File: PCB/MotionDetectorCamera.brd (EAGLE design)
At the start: 41.9 x 32.6 mm, 185 parts, among them J1 JUMPER-SOLDER, J10 MICROSD-SOCKET, J11 USB-C-JACK, J2 JUMPER-SOLDER, J3 JUMPER-SOLDER, J4 JUMPER-SOLDER, J5 JST-SM02B-SRSS-TB, J6 JUMPER-SOLDER, J7 JUMPER-SOLDER, J8 JUMPER-SOLDER, J9 S-MOUNT-LENS-HOLDERM12LENSES-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, Q1 PMOS-NEXPERIA-SOT1220, Q2 PMOS-NEXPERIA-SOT1220, Q3 PMOS-NEXPERIA-SOT1220, U1 TI-TPS2116, U10 TI-TPS22919DCK, U11 TI-TPS62A01, U13 TI-TPS22919DCK, U14 TI-TPS22919DCK, U15 TI-MSP430FR2422IRHL, U16 NXP-NTB0102, U17 NXP-NTB0102, U18 PANASONIC-EKMB110711X, U19 LATTICE-ICE40HX4K-BG121, U2 DIODESINC-AP7350, U20 WINBOND-W25Q40EW, U21 NEXPERIA-74LVC1G98-OR-INV-INP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, U22 NEXPERIA-74LVC1G98-BUFFER, U23 ON-AR0330CS1C12SPKA0, U24 ALLIANCE-AS4C8M16MSA-6BIN, U25 STM-STM32F730, U26 DIODESINC-DT1446-04V-7, U27 NEXPERIA-74LVC1G98-BUFFER, U3 NEXPERIA-74LVC1G98-NOR, U4 MICROCHIP-MCP7383X, U5 EATON-STN101, U6 TI-TPS62A01, U7 TI-TPS62A01, U9 TI-TPS22919DCK, X1 EPSON-FC-135, X2 SITIME-SIT8021, X3 SITIME-SIT8021

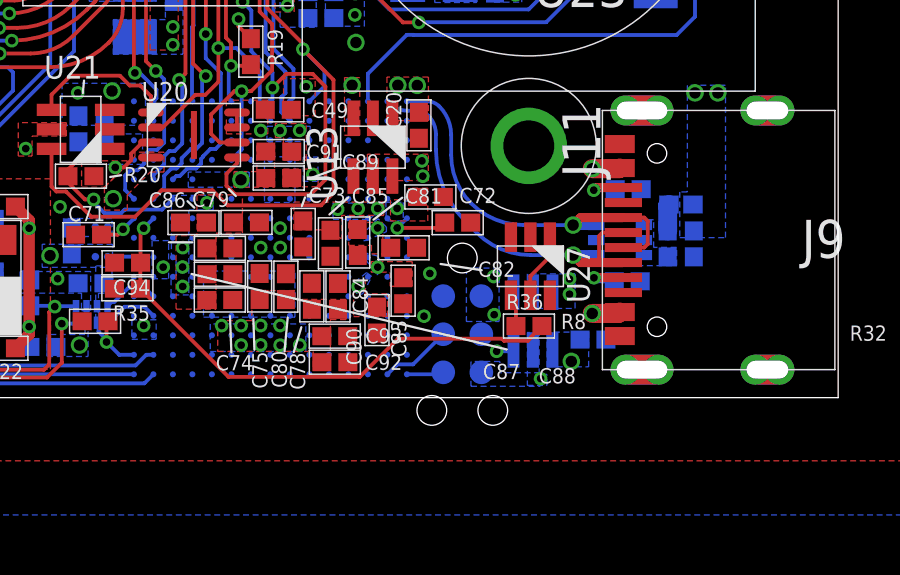
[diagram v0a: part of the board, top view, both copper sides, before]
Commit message: 39 airwires
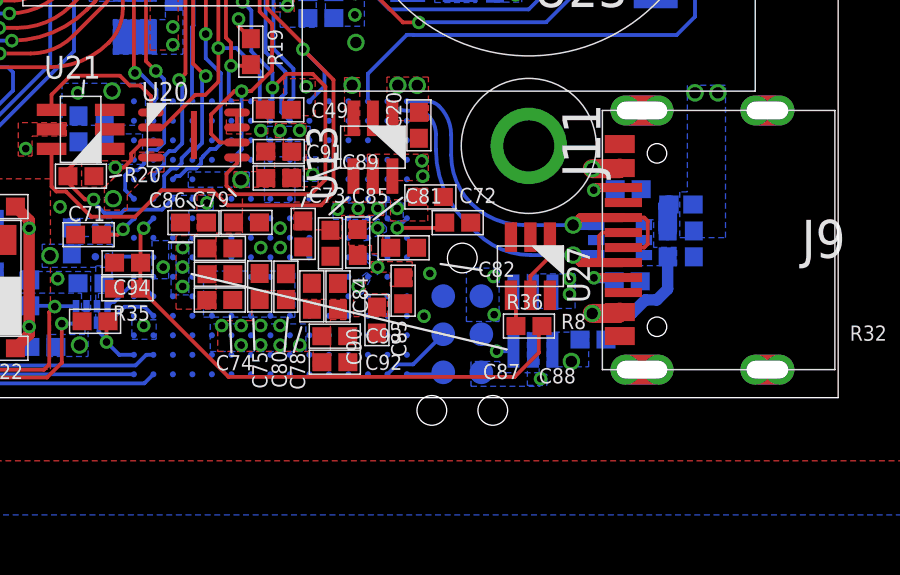
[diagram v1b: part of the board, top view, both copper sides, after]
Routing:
- net N$54: track 1.87 -> 11.4 mm
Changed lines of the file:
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@@
 <grid distance="10" unitdist="mil" unit="mil" style="lines" multiple="1" display="no" altdistance="0.00254" altunitdist="mm" altunit="mil"/>
 <layers>
-<layer number="1" name="Top" color="4" fill="1" visible="yes" active="yes"/>
+<layer number="1" name="Top" color="4" fill="1" visible="no" active="yes"/>
 <layer number="2" name="Ground" color="16" fill="1" visible="no" active="yes"/>
 <layer number="3" name="Route3" color="17" fill="1" visible="no" active="no"/>
@@
 <layer number="14" name="Route14" color="22" fill="1" visible="no" active="no"/>
 <layer number="15" name="Power" color="42" fill="1" visible="no" active="yes"/>
-<layer number="16" name="Bottom" color="1" fill="1" visible="no" active="yes"/>
+<layer number="16" name="Bottom" color="1" fill="1" visible="yes" active="yes"/>
 <layer number="17" name="Pads" color="2" fill="1" visible="yes" active="yes"/>
 <layer number="18" name="Vias" color="2" fill="1" visible="yes" active="yes"/>
 <layer number="19" name="Unrouted" color="6" fill="1" visible="no" active="yes"/>
 <layer number="20" name="Dimension" color="24" fill="1" visible="yes" active="yes"/>
-<layer number="21" name="tPlace" color="7" fill="1" visible="yes" active="yes"/>
-<layer number="22" name="bPlace" color="7" fill="1" visible="no" active="yes"/>
-<layer number="23" name="tOrigins" color="15" fill="1" visible="yes" active="yes"/>
-<layer number="24" name="bOrigins" color="15" fill="1" visible="no" active="yes"/>
-<layer number="25" name="tNames" color="7" fill="1" visible="yes" active="yes"/>
-<layer number="26" name="bNames" color="7" fill="1" visible="no" active="yes"/>
-<layer number="27" name="tValues" color="7" fill="1" visible="yes" active="yes"/>
-<layer number="28" name="bValues" color="7" fill="1" visible="no" active="yes"/>
-<layer number="29" name="tStop" color="7" fill="3" visible="yes" active="yes"/>
-<layer number="30" name="bStop" color="7" fill="6" visible="no" active="yes"/>
-<layer number="31" name="tCream" color="7" fill="4" visible="yes" active="yes"/>
-<layer number="32" name="bCream" color="7" fill="5" visible="no" active="yes"/>
-<layer number="33" name="tFinish" color="6" fill="3" visible="yes" active="yes"/>
-<layer number="34" name="bFinish" color="6" fill="6" visible="no" active="yes"/>
-<layer number="35" name="tGlue" color="7" fill="4" visible="yes" active="yes"/>
-<layer number="36" name="bGlue" color="7" fill="5" visible="no" active="yes"/>
-<layer number="37" name="tTest" color="7" fill="1" visible="yes" active="yes"/>
-<layer number="38" name="bTest" color="7" fill="1" visible="no" active="yes"/>
+<layer number="21" name="tPlace" color="7" fill="1" visible="no" active="yes"/>
+<layer number="22" name="bPlace" color="7" fill="1" visible="yes" active="yes"/>
+<layer number="23" name="tOrigins" color="15" fill="1" visible="no" active="yes"/>
+<layer number="24" name="bOrigins" color="15" fill="1" visible="yes" active="yes"/>
+<layer number="25" name="tNames" color="7" fill="1" visible="no" active="yes"/>
+<layer number="26" name="bNames" color="7" fill="1" visible="yes" active="yes"/>
+<layer number="27" name="tValues" color="7" fill="1" visible="no" active="yes"/>
+<layer number="28" name="bValues" color="7" fill="1" visible="yes" active="yes"/>
+<layer number="29" name="tStop" color="7" fill="3" visible="no" active="yes"/>
+<layer number="30" name="bStop" color="7" fill="6" visible="yes" active="yes"/>
+<layer number="31" name="tCream" color="7" fill="4" visible="no" active="yes"/>
+<layer number="32" name="bCream" color="7" fill="5" visible="yes" active="yes"/>
+<layer number="33" name="tFinish" color="6" fill="3" visible="no" active="yes"/>
+<layer number="34" name="bFinish" color="6" fill="6" visible="yes" active="yes"/>
+<layer number="35" name="tGlue" color="7" fill="4" visible="no" active="yes"/>
+<layer number="36" name="bGlue" color="7" fill="5" visible="yes" active="yes"/>
+<layer number="37" name="tTest" color="7" fill="1" visible="no" active="yes"/>
+<layer number="38" name="bTest" color="7" fill="1" visible="yes" active="yes"/>
 <layer number="39" name="tKeepout" color="4" fill="11" visible="no" active="yes"/>
 <layer number="40" name="bKeepout" color="1" fill="11" visible="no" active="yes"/>
-<layer number="41" name="tRestrict" color="4" fill="10" visible="yes" active="yes"/>
-<layer number="42" name="bRestrict" color="1" fill="10" visible="no" active="yes"/>
+<layer number="41" name="tRestrict" color="4" fill="10" visible="no" active="yes"/>
+<layer number="42" name="bRestrict" color="1" fill="10" visible="yes" active="yes"/>
 <layer number="43" name="vRestrict" color="2" fill="10" visible="no" active="yes"/>
 <layer number="44" name="Drills" color="7" fill="1" visible="no" active="yes"/>
@@
 <wire x1="26.052784375" y1="24.416325" x2="25.7902625" y2="22.882859375" width="0" layer="19" extent="16-16"/>
 <wire x1="8.56711875" y1="7.88614375" x2="9.849459375" y2="6.940978125" width="0" layer="19" extent="1-1"/>
+<wire x1="35.2575375" y1="3.878921875" x2="34.576759375" y2="2.05348125" width="0" layer="19" extent="1-16"/>
 <wire x1="-6.95095" y1="43.6726" x2="3.737384375" y2="28.8555" width="0" layer="19" extent="1-1"/>
 <wire x1="-6.95095" y1="44.5362" x2="-6.95095" y2="43.6726" width="0" layer="19" extent="1-1"/>
@@
 <wire x1="34.576759375" y1="2.85348125" x2="34.529978125" y2="2.8067" width="0.635" layer="1"/>
 <wire x1="34.529978125" y1="2.8067" x2="33.6575375" y2="2.8067" width="0.635" layer="1"/>
-<wire x1="35.38078125" y1="5.75348125" x2="34.576759375" y2="7.65348125" width="0" layer="19" extent="1-16"/>
-<wire x1="34.576759375" y1="2.85348125" x2="35.38078125" y2="4.75348125" width="0" layer="19" extent="1-16"/>
+<wire x1="33.6575375" y1="7.6327" x2="33.70071875" y2="7.58951875" width="0.635" layer="15"/>
+<wire x1="33.70071875" y1="7.58951875" x2="33.98715625" y2="7.58951875" width="0.635" layer="15"/>
+<wire x1="33.6575375" y1="2.98508125" x2="33.6575375" y2="2.8067" width="0.635" layer="15"/>
+<wire x1="34.3890625" y1="3.71660625" x2="33.6575375" y2="2.98508125" width="0.635" layer="15"/>
+<wire x1="33.98715625" y1="7.58951875" x2="34.3890625" y2="7.1876125" width="0.635" layer="15"/>
+<wire x1="34.3890625" y1="7.1876125" x2="34.3890625" y2="3.71660625" width="0.635" layer="15"/>
+<wire x1="33.6575375" y1="2.8067" x2="34.9758" y2="2.8067" width="0.381" layer="16"/>
+<wire x1="35.814" y1="3.25998125" x2="36.172684375" y2="3.618665625" width="0.381" layer="16"/>
+<wire x1="36.172684375" y1="3.618665625" x2="36.172684375" y2="4.692103125" width="0.381" layer="16"/>
+<wire x1="34.9758" y1="2.8067" x2="35.42908125" y2="3.25998125" width="0.381" layer="16"/>
+<wire x1="35.42908125" y1="3.25998125" x2="35.814" y2="3.25998125" width="0.381" layer="16"/>
 </signal>
 <signal name="MSP_TEST">
@@
 <wire x1="18.60254375" y1="4.4974375" x2="18.60254375" y2="5.545475" width="0.127" layer="1"/>
 <wire x1="18.60254375" y1="5.545475" x2="18.705403125" y2="5.648334375" width="0.127" layer="1"/>
-<wire x1="31.62425" y1="2.00779375" x2="31.51265625" y2="1.8962" width="0.127" layer="1"/>
-<wire x1="31.51265625" y1="1.8962" x2="30.71974375" y2="1.8962" width="0.127" layer="1"/>
-<wire x1="31.9812" y1="2.3867" x2="31.62425" y2="2.02975" width="0.127" layer="1"/>
-<wire x1="31.62425" y1="2.02975" x2="31.62425" y2="2.00779375" width="0.127" layer="1"/>
-<wire x1="30.71974375" y1="1.8962" x2="30.64998125" y2="1.9659625" width="0.127" layer="1"/>
-<wire x1="30.64998125" y1="1.9659625" x2="27.1823375" y2="1.9659625" width="0.127" layer="1"/>
-<wire x1="27.1823375" y1="1.9659625" x2="25.9082875" y2="0.6919125" width="0.127" layer="1"/>
-<wire x1="25.9082875" y1="0.6919125" x2="21.53454375" y2="0.6919125" width="0.127" layer="1"/>
+<wire x1="31.87825" y1="1.49979375" x2="31.07036875" y2="0.6919125" width="0.127" layer="1"/>
+<wire x1="31.9812" y1="2.3867" x2="31.87825" y2="2.28375" width="0.127" layer="1"/>
+<wire x1="31.87825" y1="2.28375" x2="31.87825" y2="1.49979375" width="0.127" layer="1"/>
+<wire x1="31.07036875" y1="0.6919125" x2="21.53454375" y2="0.6919125" width="0.127" layer="1"/>
 <wire x1="21.53454375" y1="0.6919125" x2="18.595159375" y2="3.631296875" width="0.127" layer="1"/>
 <wire x1="18.595159375" y1="3.631296875" x2="18.595159375" y2="4.490053125" width="0.127" layer="1"/>

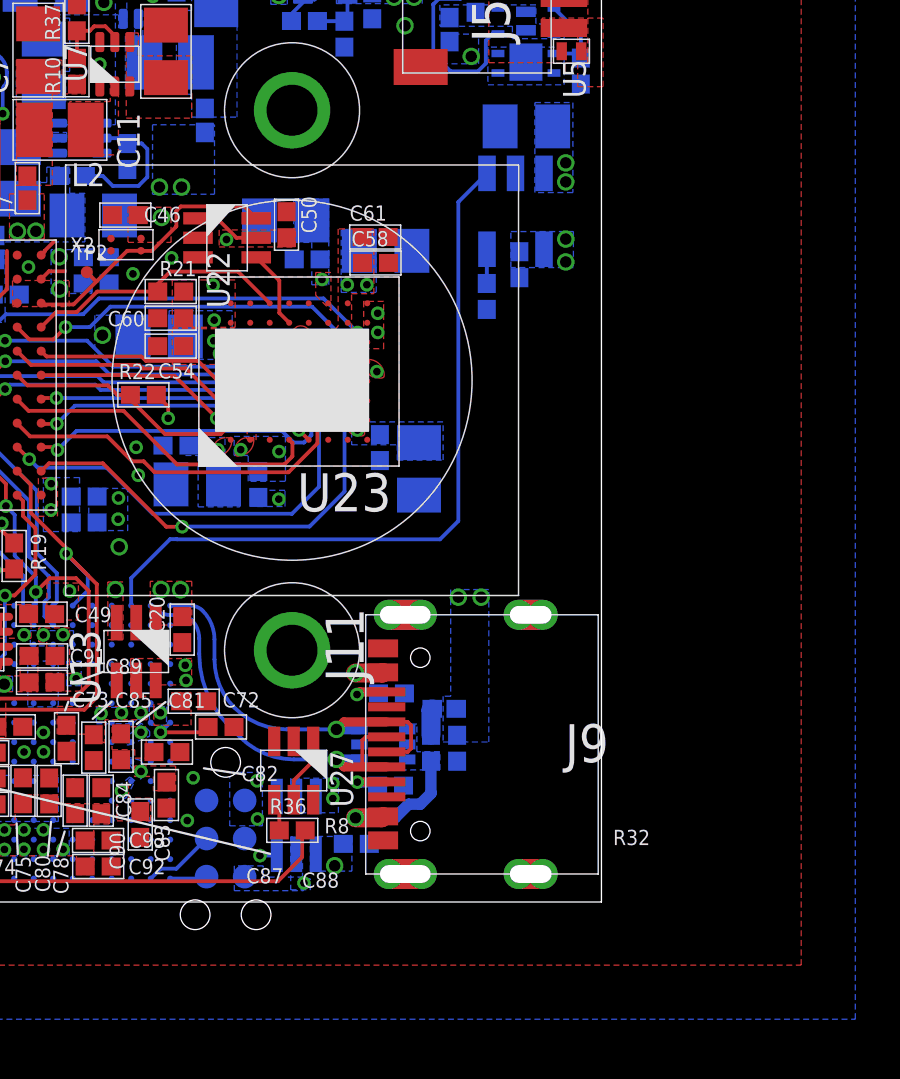
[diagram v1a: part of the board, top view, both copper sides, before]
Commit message: 38 airwires
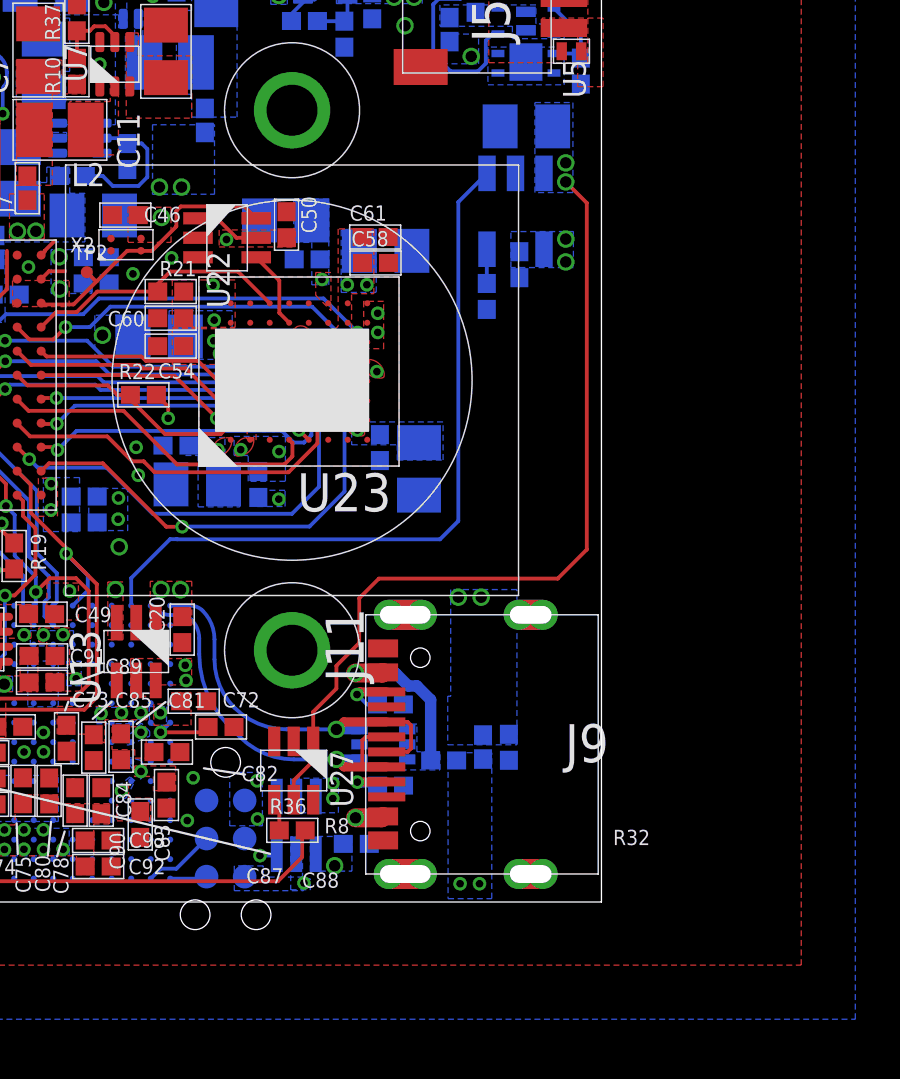
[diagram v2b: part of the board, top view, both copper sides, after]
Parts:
- moved J1 1.82 mm to (37.9, 5.16), turned to 90 degrees
- moved R1 1.73 mm to (38.8, 5.16)
- moved FB1 0.59 mm to (36.6, 4.72), turned to 180 degrees
- moved R34 0.37 mm to (34.8, 6.58)
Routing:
- net VDD_BAT: track 8.33 -> 34.5 mm
- net VDD_USB_IN: track 0.90 -> 11.5 mm, vias 2 -> 4
- net N$54: track 11.4 -> 12.4 mm

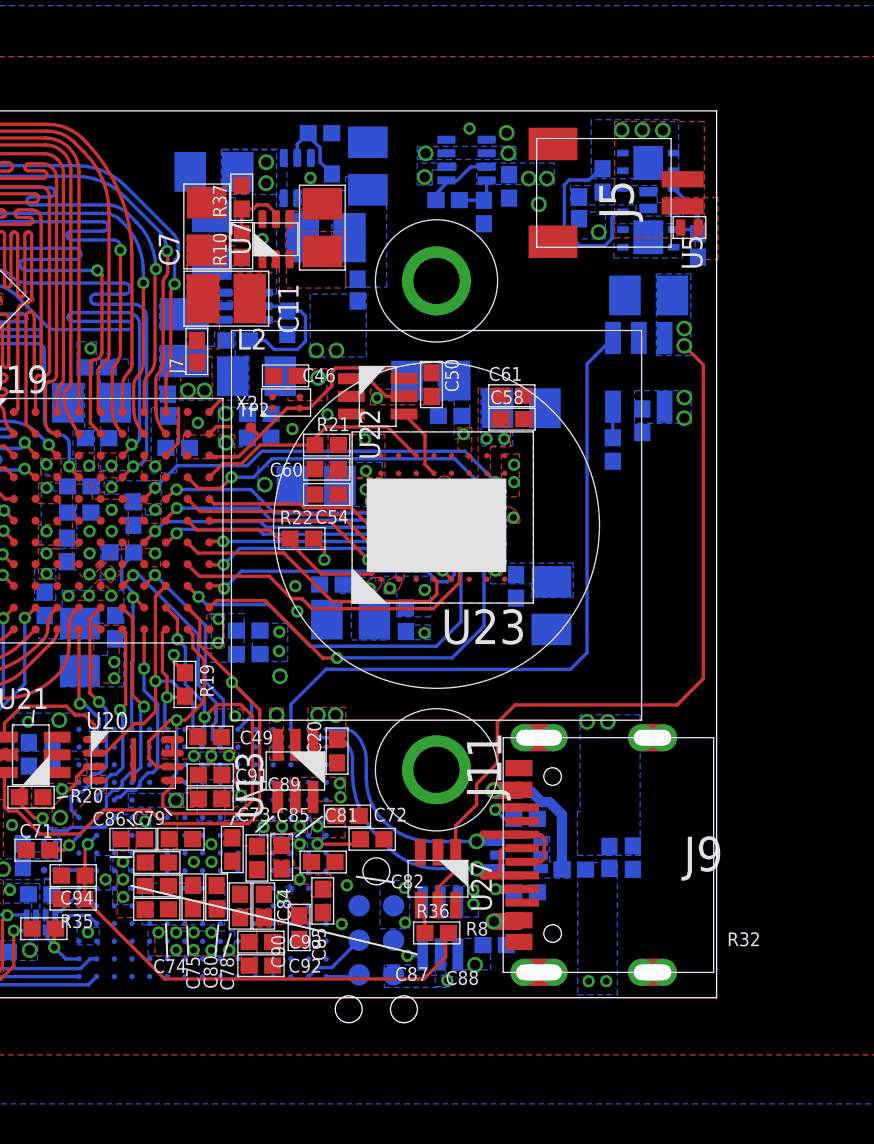
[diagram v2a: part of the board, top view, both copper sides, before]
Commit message: 36 airwires
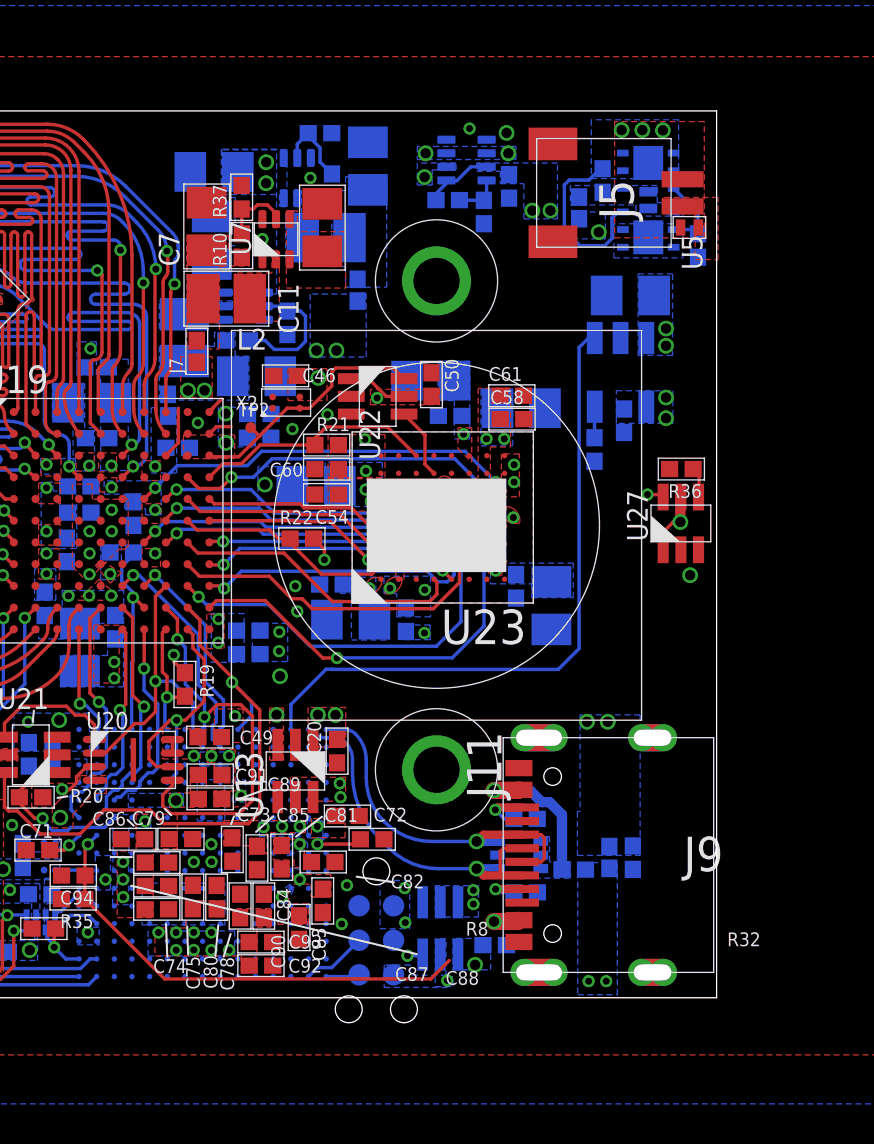
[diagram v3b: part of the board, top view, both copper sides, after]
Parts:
- moved R36 19.3 mm to (40.6, 19.5), turned to 180 degrees
- moved U27 15.8 mm to (40.5, 17.5), turned to 90 degrees
- moved C5 0.67 mm to (38.4, 21.2)
- moved C6 0.67 mm to (38.7, 25.9)
- moved R5 0.67 mm to (37.4, 20.2)
- moved U4 0.67 mm to (38.3, 23.0)
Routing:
- net VDD_BAT: track 34.5 -> 21.8 mm, vias 4 -> 5
- net VDD_USB: track 39.6 -> 38.6 mm, vias 7 -> 8
- net BAT_CHRG_LVL: track 18.3 -> 17.4 mm
